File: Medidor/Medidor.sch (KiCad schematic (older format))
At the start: 47 parts, among them J1 TC2030-CTX-TAG_CONECT, SW1 Rotary_Encoder_Switch, SW2 SW_DPST_x2, U1 INA219-INA, U2 Serial, X1 32MHz

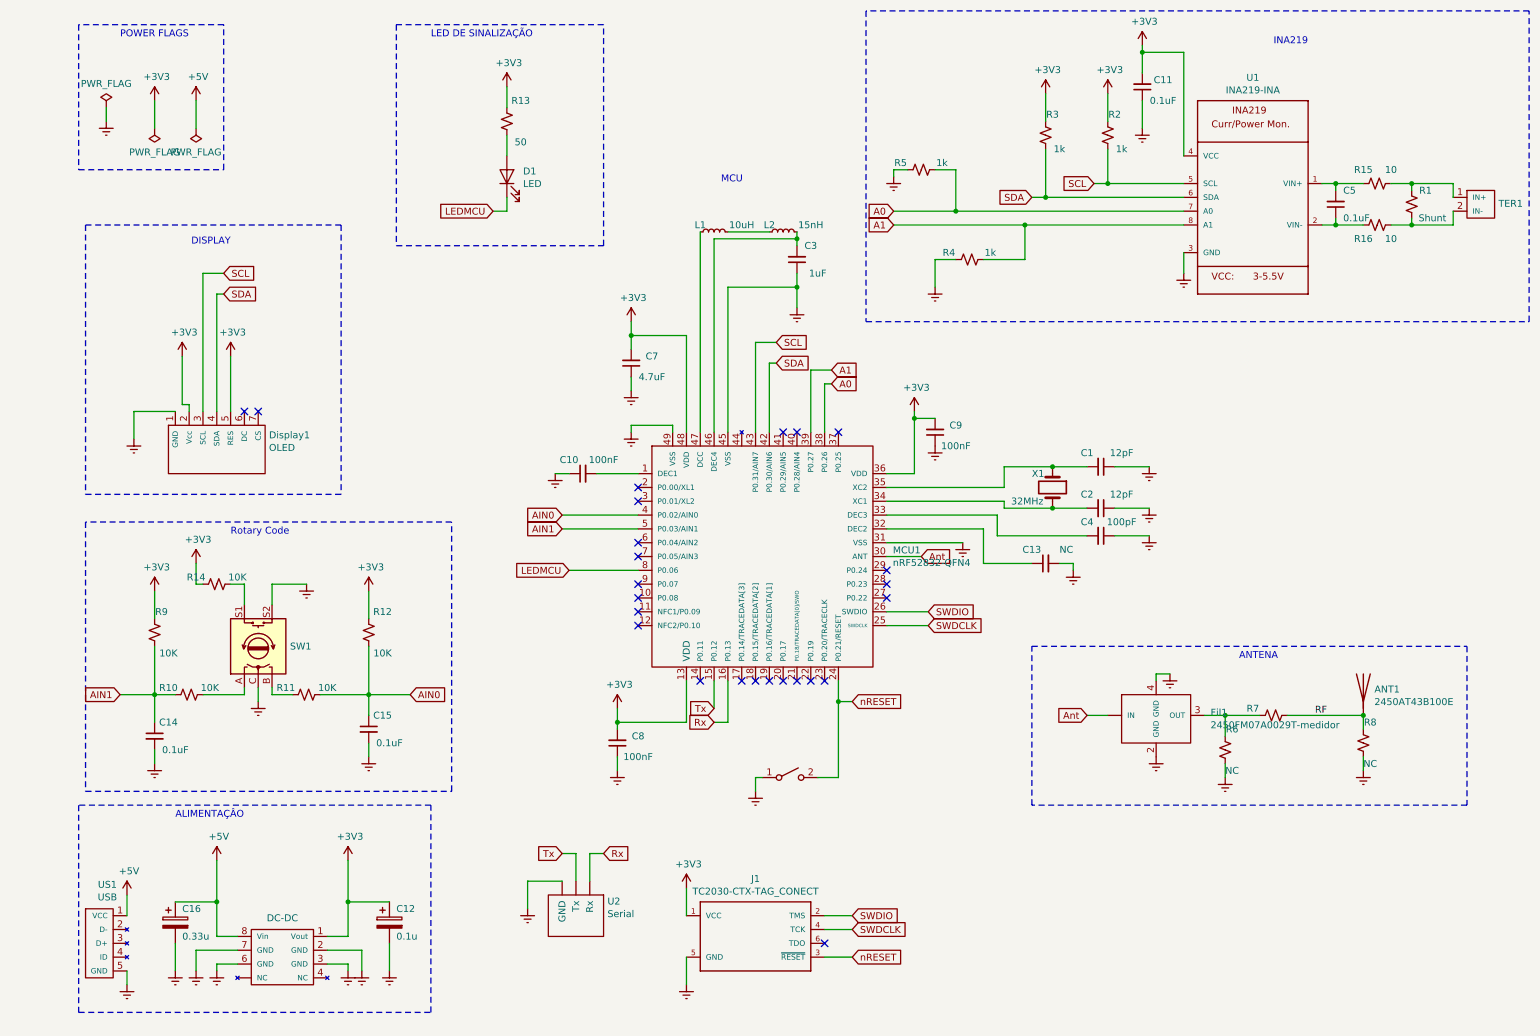
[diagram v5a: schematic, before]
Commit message: Add ohm symbol
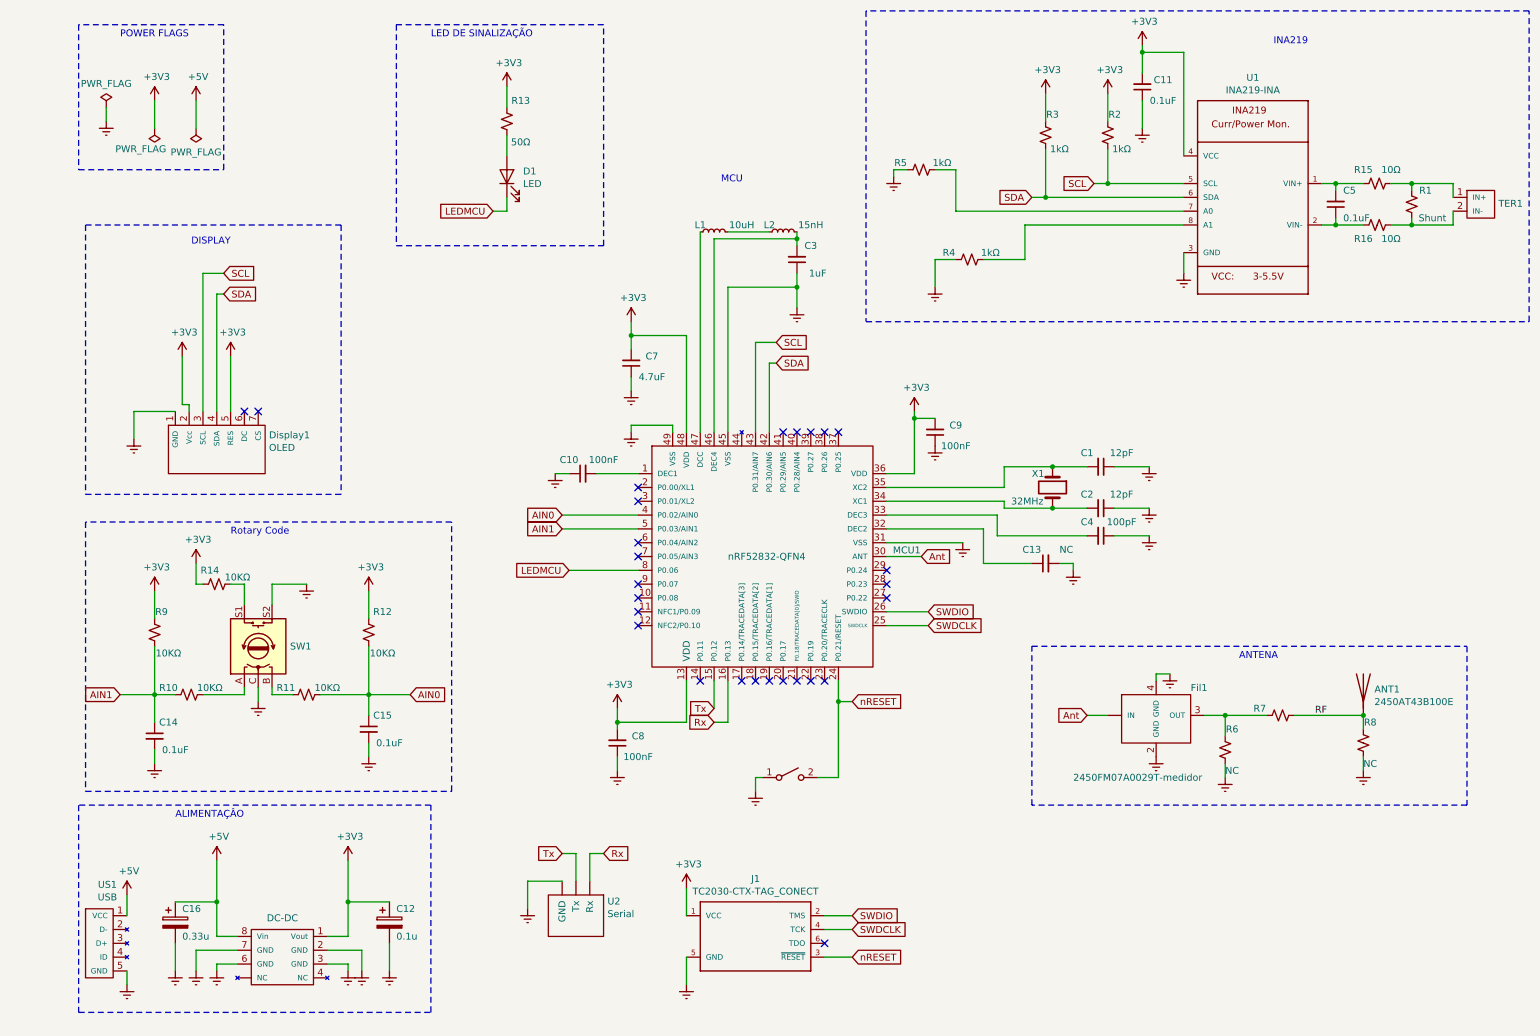
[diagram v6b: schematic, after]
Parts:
- R10, R11, R12, R14, R9: value 10K -> 10KΩ
- R13: value 50 -> 50Ω
- R15, R16: value 10 -> 10Ω
- R2, R3, R4, R5: value 1k -> 1kΩ
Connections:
- net A0: no longer names the net of R5.2, U1.7 (A0)
- net A0: no longer MCU1.38 (P0.26)
- net A1: no longer names the net of R4.2, U1.8 (A1)
- net A1: no longer MCU1.39 (P0.27)
- no-connect marks 25 -> 27
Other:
- moved on the sheet: R7
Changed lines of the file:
@@
 P 1250 1350
 F 0 "#FLG0102" H 1250 1425 50  0001 C CNN
-F 1 "PWR_FLAG" H 1250 1523 50  0000 C CNN
+F 1 "PWR_FLAG" H 1350 1500 50  0000 C CNN
 F 2 "" H 1250 1350 50  0001 C CNN
 F 3 "~" H 1250 1350 50  0001 C CNN
@@
 P 8150 1400
 F 0 "R2" H 8100 1250 50  0000 C CNN
-F 1 "1k" H 8050 1500 50  0000 C CNN
+F 1 "1kΩ" H 8050 1500 50  0000 C CNN
 F 2 "" H 8150 1400 50  0001 C CNN
 F 3 "~" H 8150 1400 50  0001 C CNN
@@
 P 7700 1400
 F 0 "R3" H 7650 1250 50  0000 C CNN
-F 1 "1k" H 7600 1500 50  0000 C CNN
+F 1 "1kΩ" H 7600 1500 50  0000 C CNN
 F 2 "" H 7700 1400 50  0001 C CNN
 F 3 "~" H 7700 1400 50  0001 C CNN
@@
 P 7150 2300
 F 0 "R4" V 7200 2450 50  0000 C CNN
-F 1 "1k" V 7200 2150 50  0000 C CNN
+F 1 "1kΩ" V 7200 2150 50  0000 C CNN
 F 2 "" H 7150 2300 50  0001 C CNN
 F 3 "~" H 7150 2300 50  0001 C CNN
@@
 P 6800 1650
 F 0 "R5" V 6850 1800 50  0000 C CNN
-F 1 "1k" V 6850 1500 50  0000 C CNN
+F 1 "1kΩ" V 6850 1500 50  0000 C CNN
 F 2 "" H 6800 1650 50  0001 C CNN
 F 3 "~" H 6800 1650 50  0001 C CNN
@@
 	9000 5750 9000 5600
 Wire Wire Line
-	9250 5600 9000 5600
+	9300 5600 9000 5600
 $Comp
 L power:Earth #PWR0110
@@
 Wire Wire Line
 	6550 4950 6850 4950
-Connection ~ 7550 2050
-Text GLabel 6600 2050 0    50   Input ~ 0
-A1
-Wire Wire Line
-	6600 2050 7550 2050
-Text GLabel 6600 1950 0    50   Input ~ 0
-A0
 Wire Wire Line
 	6600 1700 6600 1650
@@
 	6600 1650 6700 1650
 Wire Wire Line
-	6600 1950 7050 1950
-Wire Wire Line
 	6900 1650 7050 1650
 Wire Wire Line
 	7050 1650 7050 1950
-Connection ~ 7050 1950
 Wire Wire Line
 	7050 1950 8700 1950
@@
 Wire Wire Line
 	6900 2300 7050 2300
-Text GLabel 6150 3200 2    50   Input ~ 0
-A0
-Wire Wire Line
-	6150 3200 6100 3200
-Wire Wire Line
-	6100 3200 6100 3550
-Text GLabel 6150 3100 2    50   Input ~ 0
-A1
-Wire Wire Line
-	6150 3100 6000 3100
-Wire Wire Line
-	6000 3100 6000 3550
 $Comp
 L Device:R_Small_US R7
 U 1 1 5D3AD244
-P 9350 5600
-F 0 "R7" V 9400 5750 50  0000 C CNN
-F 1 "1k" V 9400 5450 50  0001 C CNN
-F 2 "" H 9350 5600 50  0001 C CNN
-F 3 "~" H 9350 5600 50  0001 C CNN
-	1    9350 5600
+P 9400 5600
+F 0 "R7" V 9450 5750 50  0000 C CNN
+F 1 "1k" V 9450 5450 50  0001 C CNN
+F 2 "" H 9400 5600 50  0001 C CNN
+F 3 "~" H 9400 5600 50  0001 C CNN
+	1    9400 5600
 	0    -1   -1   0
 $EndComp
@@
 	9000 6050 9000 5950
 Wire Wire Line
-	9450 5600 10000 5600
+	9500 5600 10000 5600
 $Comp
 L Device:R_Small_US R8
@@
 P 1250 5000
 F 0 "R9" H 1300 5150 50  0000 C CNN
-F 1 "10K" H 1350 4850 50  0000 C CNN
+F 1 "10KΩ" H 1350 4850 50  0000 C CNN
 F 2 "" H 1250 5000 50  0001 C CNN
 F 3 "~" H 1250 5000 50  0001 C CNN
@@
 P 1500 5450
 F 0 "R10" V 1550 5600 50  0000 C CNN
-F 1 "10K" V 1550 5300 50  0000 C CNN
+F 1 "10KΩ" V 1550 5300 50  0000 C CNN
 F 2 "" H 1500 5450 50  0001 C CNN
 F 3 "~" H 1500 5450 50  0001 C CNN
@@
 P 2350 5450
 F 0 "R11" V 2400 5600 50  0000 C CNN
-F 1 "10K" V 2400 5300 50  0000 C CNN
+F 1 "10KΩ" V 2400 5300 50  0000 C CNN
 F 2 "" H 2350 5450 50  0001 C CNN
 F 3 "~" H 2350 5450 50  0001 C CNN
@@
 P 2800 5000
 F 0 "R12" H 2900 5150 50  0000 C CNN
-F 1 "10K" H 2900 4850 50  0000 C CNN
+F 1 "10KΩ" H 2900 4850 50  0000 C CNN
 F 2 "" H 2800 5000 50  0001 C CNN
 F 3 "~" H 2800 5000 50  0001 C CNN
@@
 P 3800 1300
 F 0 "R13" H 3700 1150 50  0000 C CNN
-F 1 "50" H 3700 1450 50  0000 C CNN
+F 1 "50Ω" H 3700 1450 50  0000 C CNN
 F 2 "" H 3800 1300 50  0001 C CNN
 F 3 "~" H 3800 1300 50  0001 C CNN
@@
 P 5650 4400
 F 0 "MCU1" H 6594 4396 50  0000 L CNN
-F 1 "nRF52832-QFN4" H 6594 4305 50  0000 L CNN
+F 1 "nRF52832-QFN4" H 5400 4350 50  0000 L CNN
 F 2 "" H 4650 6050 50  0001 C CNN
 F 3 "" H 4650 6050 50  0001 C CNN
@@
 U 1 1 5D5CC96B
 P 8500 5600
-F 0 "Fil1" H 8894 5621 50  0000 L CNN
-F 1 "2450FM07A0029T-medidor" H 8894 5530 50  0000 L CNN
+F 0 "Fil1" H 8750 5800 50  0000 L CNN
+F 1 "2450FM07A0029T-medidor" H 7900 5150 50  0000 L CNN
 F 2 "" H 8500 5600 50  0001 C CNN
 F 3 "" H 8500 5600 50  0001 C CNN
@@
 U 1 1 5D352B3E
 P 1700 4650
-F 0 "R14" V 1750 4800 50  0000 C CNN
-F 1 "10K" V 1750 4500 50  0000 C CNN
+F 0 "R14" V 1800 4700 50  0000 C CNN
+F 1 "10KΩ" V 1750 4500 50  0000 C CNN
 F 2 "" H 1700 4650 50  0001 C CNN
 F 3 "~" H 1700 4650 50  0001 C CNN
@@
 P 10100 2050
 F 0 "R16" V 10200 1950 50  0000 C CNN
-F 1 "10" V 10200 2150 50  0000 C CNN
+F 1 "10Ω" V 10200 2150 50  0000 C CNN
 F 2 "" H 10100 2050 50  0001 C CNN
 F 3 "~" H 10100 2050 50  0001 C CNN
@@
 P 10100 1750
 F 0 "R15" V 10000 1650 50  0000 C CNN
-F 1 "10" V 10000 1850 50  0000 C CNN
+F 1 "10Ω" V 10000 1850 50  0000 C CNN
 F 2 "" H 10100 1750 50  0001 C CNN
 F 3 "~" H 10100 1750 50  0001 C CNN
@@
 Wire Wire Line
 	9800 2050 10000 2050
+NoConn ~ 6100 3550
+NoConn ~ 6000 3550
 $EndSCHEMATC

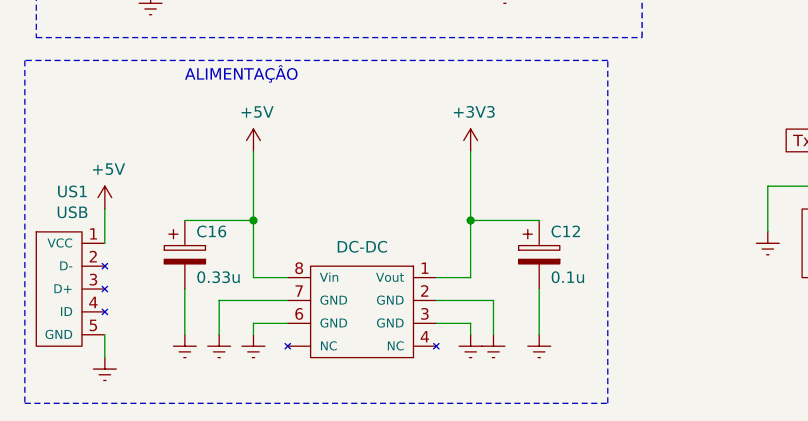
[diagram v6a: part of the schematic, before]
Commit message: Adicionando alguns footprints
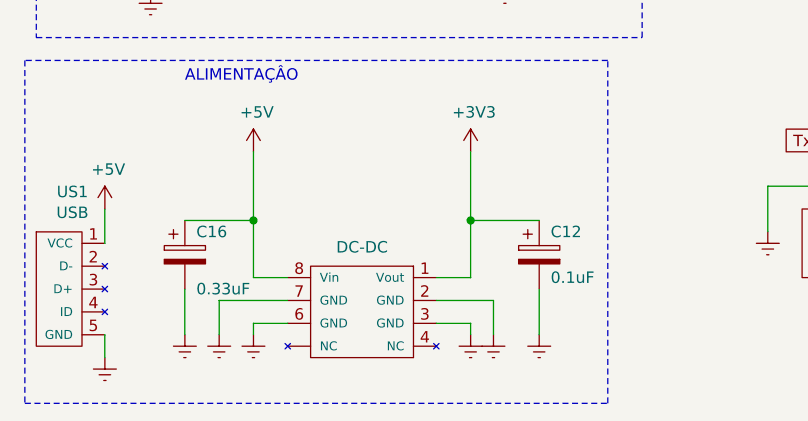
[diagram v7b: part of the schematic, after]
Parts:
- C1, C10, C11, C13, C14, C15, C2, C3, C4, C5, C8, C9: footprint (none) -> Capacitor_SMD:C_0402_1005Metric
- C12: value 0.1u -> 0.1uF; footprint (none) -> Capacitor_SMD:CP_Elec_4x3
- C16: value 0.33u -> 0.33uF; footprint (none) -> Capacitor_SMD:CP_Elec_4x3
- C7: footprint (none) -> Capacitor_SMD:C_0603_1608Metric
- Display1: footprint (none) -> Medidor:OLED
- L1: footprint (none) -> Inductor_SMD:L_0603_1608Metric
- L2: footprint (none) -> Inductor_SMD:L_0402_1005Metric
- MCU1: footprint (none) -> Package_DFN_QFN:QFN-48-1EP_6x6mm_P0.4mm_EP4.2x4.2mm
- R10, R11, R12, R13, R14, R15, R16, R2, R3, R4, R5, R6, R7, R8, R9: footprint (none) -> Resistor_SMD:R_0402_1005Metric
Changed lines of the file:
@@
 F 0 "C1" V 8000 3700 50  0000 C CNN
 F 1 "12pF" V 8000 3950 50  0000 C CNN
-F 2 "" H 8100 3800 50  0001 C CNN
+F 2 "Capacitor_SMD:C_0402_1005Metric" H 8100 3800 50  0001 C CNN
 F 3 "~" H 8100 3800 50  0001 C CNN
 	1    8100 3800
@@
 F 0 "C2" V 8000 4000 50  0000 C CNN
 F 1 "12pF" V 8000 4250 50  0000 C CNN
-F 2 "" H 8100 4100 50  0001 C CNN
+F 2 "Capacitor_SMD:C_0402_1005Metric" H 8100 4100 50  0001 C CNN
 F 3 "~" H 8100 4100 50  0001 C CNN
 	1    8100 4100
@@
 F 0 "L1" V 5350 2200 50  0000 C CNN
 F 1 "10uH" V 5350 1900 50  0000 C CNN
-F 2 "" H 5300 2100 50  0001 C CNN
+F 2 "Inductor_SMD:L_0603_1608Metric" H 5300 2100 50  0001 C CNN
 F 3 "~" H 5300 2100 50  0001 C CNN
 	1    5300 2100
@@
 F 0 "L2" V 5850 2200 50  0000 C CNN
 F 1 "15nH" V 5850 1900 50  0000 C CNN
-F 2 "" H 5800 2100 50  0001 C CNN
+F 2 "Inductor_SMD:L_0402_1005Metric" H 5800 2100 50  0001 C CNN
 F 3 "~" H 5800 2100 50  0001 C CNN
 	1    5800 2100
@@
 F 0 "C3" H 5800 2200 50  0000 C CNN
 F 1 "1uF" H 5750 2400 50  0000 C CNN
-F 2 "" H 5900 2300 50  0001 C CNN
+F 2 "Capacitor_SMD:C_0402_1005Metric" H 5900 2300 50  0001 C CNN
 F 3 "~" H 5900 2300 50  0001 C CNN
 	1    5900 2300
@@
 F 0 "C4" V 8000 4200 50  0000 C CNN
 F 1 "100pF" V 8000 4450 50  0000 C CNN
-F 2 "" H 8100 4300 50  0001 C CNN
+F 2 "Capacitor_SMD:C_0402_1005Metric" H 8100 4300 50  0001 C CNN
 F 3 "~" H 8100 4300 50  0001 C CNN
 	1    8100 4300
@@
 F 0 "C7" H 4550 3000 50  0000 C CNN
 F 1 "4.7uF" H 4550 3150 50  0000 C CNN
-F 2 "" H 4700 3050 50  0001 C CNN
+F 2 "Capacitor_SMD:C_0603_1608Metric" H 4700 3050 50  0001 C CNN
 F 3 "~" H 4700 3050 50  0001 C CNN
 	1    4700 3050
@@
 F 0 "C8" H 4450 5750 50  0000 C CNN
 F 1 "100nF" H 4450 5900 50  0000 C CNN
-F 2 "" H 4600 5800 50  0001 C CNN
+F 2 "Capacitor_SMD:C_0402_1005Metric" H 4600 5800 50  0001 C CNN
 F 3 "~" H 4600 5800 50  0001 C CNN
 	1    4600 5800
@@
 F 0 "C9" H 6750 3500 50  0000 C CNN
 F 1 "100nF" H 6750 3650 50  0000 C CNN
-F 2 "" H 6900 3550 50  0001 C CNN
+F 2 "Capacitor_SMD:C_0402_1005Metric" H 6900 3550 50  0001 C CNN
 F 3 "~" H 6900 3550 50  0001 C CNN
 	1    6900 3550
@@
 F 0 "C10" V 4450 3950 50  0000 C CNN
 F 1 "100nF" V 4450 3700 50  0000 C CNN
-F 2 "" H 4350 3850 50  0001 C CNN
+F 2 "Capacitor_SMD:C_0402_1005Metric" H 4350 3850 50  0001 C CNN
 F 3 "~" H 4350 3850 50  0001 C CNN
 	1    4350 3850
@@
 F 0 "R2" H 8100 1250 50  0000 C CNN
 F 1 "1kΩ" H 8050 1500 50  0000 C CNN
-F 2 "" H 8150 1400 50  0001 C CNN
+F 2 "Resistor_SMD:R_0402_1005Metric" H 8150 1400 50  0001 C CNN
 F 3 "~" H 8150 1400 50  0001 C CNN
 	1    8150 1400
@@
 F 0 "C11" H 8250 1000 50  0000 C CNN
 F 1 "0.1uF" H 8250 1150 50  0000 C CNN
-F 2 "" H 8400 1050 50  0001 C CNN
+F 2 "Capacitor_SMD:C_0402_1005Metric" H 8400 1050 50  0001 C CNN
 F 3 "~" H 8400 1050 50  0001 C CNN
 	1    8400 1050
@@
 F 0 "R3" H 7650 1250 50  0000 C CNN
 F 1 "1kΩ" H 7600 1500 50  0000 C CNN
-F 2 "" H 7700 1400 50  0001 C CNN
+F 2 "Resistor_SMD:R_0402_1005Metric" H 7700 1400 50  0001 C CNN
 F 3 "~" H 7700 1400 50  0001 C CNN
 	1    7700 1400
@@
 F 0 "R4" V 7200 2450 50  0000 C CNN
 F 1 "1kΩ" V 7200 2150 50  0000 C CNN
-F 2 "" H 7150 2300 50  0001 C CNN
+F 2 "Resistor_SMD:R_0402_1005Metric" H 7150 2300 50  0001 C CNN
 F 3 "~" H 7150 2300 50  0001 C CNN
 	1    7150 2300
@@
 F 0 "R5" V 6850 1800 50  0000 C CNN
 F 1 "1kΩ" V 6850 1500 50  0000 C CNN
-F 2 "" H 6800 1650 50  0001 C CNN
+F 2 "Resistor_SMD:R_0402_1005Metric" H 6800 1650 50  0001 C CNN
 F 3 "~" H 6800 1650 50  0001 C CNN
 	1    6800 1650
@@
 P 2950 7100
 F 0 "C12" H 3000 7200 50  0000 L CNN
-F 1 "0.1u" H 3000 7000 50  0000 L CNN
-F 2 "" H 2988 6950 50  0001 C CNN
+F 1 "0.1uF" H 3000 7000 50  0000 L CNN
+F 2 "Capacitor_SMD:CP_Elec_4x3" H 2988 6950 50  0001 C CNN
 F 3 "~" H 2950 7100 50  0001 C CNN
 	1    2950 7100
@@
 F 0 "R7" V 9450 5750 50  0000 C CNN
 F 1 "1k" V 9450 5450 50  0001 C CNN
-F 2 "" H 9400 5600 50  0001 C CNN
+F 2 "Resistor_SMD:R_0402_1005Metric" H 9400 5600 50  0001 C CNN
 F 3 "~" H 9400 5600 50  0001 C CNN
 	1    9400 5600
@@
 F 0 "R6" H 9050 6000 50  0000 C CNN
 F 1 "NC" H 9050 5700 50  0000 C CNN
-F 2 "" H 9000 5850 50  0001 C CNN
+F 2 "Resistor_SMD:R_0402_1005Metric" H 9000 5850 50  0001 C CNN
 F 3 "~" H 9000 5850 50  0001 C CNN
 	1    9000 5850
@@
 F 0 "R8" H 10050 5950 50  0000 C CNN
 F 1 "NC" H 10050 5650 50  0000 C CNN
-F 2 "" H 10000 5800 50  0001 C CNN
+F 2 "Resistor_SMD:R_0402_1005Metric" H 10000 5800 50  0001 C CNN
 F 3 "~" H 10000 5800 50  0001 C CNN
 	1    10000 5800
@@
 F 0 "C13" V 7800 4600 50  0000 C CNN
 F 1 "NC" V 7800 4350 50  0000 C CNN
-F 2 "" H 7700 4500 50  0001 C CNN
+F 2 "Capacitor_SMD:C_0402_1005Metric" H 7700 4500 50  0001 C CNN
 F 3 "~" H 7700 4500 50  0001 C CNN
 	1    7700 4500
@@
 F 0 "R9" H 1300 5150 50  0000 C CNN
 F 1 "10KΩ" H 1350 4850 50  0000 C CNN
-F 2 "" H 1250 5000 50  0001 C CNN
+F 2 "Resistor_SMD:R_0402_1005Metric" H 1250 5000 50  0001 C CNN
 F 3 "~" H 1250 5000 50  0001 C CNN
 	1    1250 5000
@@
 F 0 "R10" V 1550 5600 50  0000 C CNN
 F 1 "10KΩ" V 1550 5300 50  0000 C CNN
-F 2 "" H 1500 5450 50  0001 C CNN
+F 2 "Resistor_SMD:R_0402_1005Metric" H 1500 5450 50  0001 C CNN
 F 3 "~" H 1500 5450 50  0001 C CNN
 	1    1500 5450
@@
 F 0 "C14" H 1350 5850 50  0000 C CNN
 F 1 "0.1uF" H 1400 5650 50  0000 C CNN
-F 2 "" H 1250 5750 50  0001 C CNN
+F 2 "Capacitor_SMD:C_0402_1005Metric" H 1250 5750 50  0001 C CNN
 F 3 "~" H 1250 5750 50  0001 C CNN
 	1    1250 5750
@@
 F 0 "R11" V 2400 5600 50  0000 C CNN
 F 1 "10KΩ" V 2400 5300 50  0000 C CNN
-F 2 "" H 2350 5450 50  0001 C CNN
+F 2 "Resistor_SMD:R_0402_1005Metric" H 2350 5450 50  0001 C CNN
 F 3 "~" H 2350 5450 50  0001 C CNN
 	1    2350 5450
@@
 F 0 "R12" H 2900 5150 50  0000 C CNN
 F 1 "10KΩ" H 2900 4850 50  0000 C CNN
-F 2 "" H 2800 5000 50  0001 C CNN
+F 2 "Resistor_SMD:R_0402_1005Metric" H 2800 5000 50  0001 C CNN
 F 3 "~" H 2800 5000 50  0001 C CNN
 	1    2800 5000
@@
 F 0 "C15" H 2900 5800 50  0000 C CNN
 F 1 "0.1uF" H 2950 5600 50  0000 C CNN
-F 2 "" H 2800 5700 50  0001 C CNN
+F 2 "Capacitor_SMD:C_0402_1005Metric" H 2800 5700 50  0001 C CNN
 F 3 "~" H 2800 5700 50  0001 C CNN
 	1    2800 5700
@@
 F 0 "R13" H 3700 1150 50  0000 C CNN
 F 1 "50Ω" H 3700 1450 50  0000 C CNN
-F 2 "" H 3800 1300 50  0001 C CNN
+F 2 "Resistor_SMD:R_0402_1005Metric" H 3800 1300 50  0001 C CNN
 F 3 "~" H 3800 1300 50  0001 C CNN
 	1    3800 1300
@@
 P 1400 7100
 F 0 "C16" H 1450 7200 50  0000 L CNN
-F 1 "0.33u" H 1450 7000 50  0000 L CNN
-F 2 "" H 1438 6950 50  0001 C CNN
+F 1 "0.33uF" H 1450 6950 50  0000 L CNN
+F 2 "Capacitor_SMD:CP_Elec_4x3" H 1438 6950 50  0001 C CNN
 F 3 "~" H 1400 7100 50  0001 C CNN
 	1    1400 7100
@@
 F 0 "MCU1" H 6594 4396 50  0000 L CNN
 F 1 "nRF52832-QFN4" H 5400 4350 50  0000 L CNN
-F 2 "" H 4650 6050 50  0001 C CNN
+F 2 "Package_DFN_QFN:QFN-48-1EP_6x6mm_P0.4mm_EP4.2x4.2mm" H 4650 6050 50  0001 C CNN
 F 3 "" H 4650 6050 50  0001 C CNN
 	1    5650 4400
@@
 F 0 "Display1" H 2078 3829 50  0000 L CNN
 F 1 "OLED" H 2078 3738 50  0000 L CNN
-F 2 "" H 1700 3700 50  0001 C CNN
+F 2 "Medidor:OLED" H 1700 3700 50  0001 C CNN
 F 3 "" H 1700 3700 50  0001 C CNN
 	1    1700 3700
@@
 F 0 "R14" V 1800 4700 50  0000 C CNN
 F 1 "10KΩ" V 1750 4500 50  0000 C CNN
-F 2 "" H 1700 4650 50  0001 C CNN
+F 2 "Resistor_SMD:R_0402_1005Metric" H 1700 4650 50  0001 C CNN
 F 3 "~" H 1700 4650 50  0001 C CNN
 	1    1700 4650
@@
 F 0 "R16" V 10200 1950 50  0000 C CNN
 F 1 "10Ω" V 10200 2150 50  0000 C CNN
-F 2 "" H 10100 2050 50  0001 C CNN
+F 2 "Resistor_SMD:R_0402_1005Metric" H 10100 2050 50  0001 C CNN
 F 3 "~" H 10100 2050 50  0001 C CNN
 	1    10100 2050
@@
 F 0 "R15" V 10000 1650 50  0000 C CNN
 F 1 "10Ω" V 10000 1850 50  0000 C CNN
-F 2 "" H 10100 1750 50  0001 C CNN
+F 2 "Resistor_SMD:R_0402_1005Metric" H 10100 1750 50  0001 C CNN
 F 3 "~" H 10100 1750 50  0001 C CNN
 	1    10100 1750
@@
 F 0 "C5" H 9700 1800 50  0000 C CNN
 F 1 "0.1uF" H 9650 2000 50  0000 C CNN
-F 2 "" H 9800 1900 50  0001 C CNN
+F 2 "Capacitor_SMD:C_0402_1005Metric" H 9800 1900 50  0001 C CNN
 F 3 "~" H 9800 1900 50  0001 C CNN
 	1    9800 1900
